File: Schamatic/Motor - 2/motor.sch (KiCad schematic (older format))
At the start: 60 parts, among them J1 CONN_02X05, J11 V, J12 U, J13 W, J3 RS485, J6 +BAT, J9 GND, Q1 PSMN3R3-40YS, Q2 PSMN3R3-40YS, Q3 PSMN3R3-40YS, Q4 PSMN3R3-40YS, Q5 PSMN3R3-40YS, Q6 PSMN3R3-40YS, Q7 NTR5103N, SW1 B3U-1000P, SW2 B3U-1000P, U1 MAX17502, U2 LTC2876, U3 MA700, U4 LM5019, U5 STM32F031K6U6, U6 AUIRS20302, Y1 8MhZ

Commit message: progress
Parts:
- removed C12: 3300pF, Capacitors_SMD:C_0603, symbol C_Small
- removed C13: 22uF, Capacitors_SMD:C_0805, symbol C_Small
- removed C8: 0.1uF, Capacitors_SMD:C_0603, symbol C_Small
- removed L1: 15uH, Inductors_SMD:L_1210, symbol L_Small
- removed U1: MAX17502, Housings_DFN_QFN:DFN-10-1EP_2x3mm_Pitch0.5mm, symbol MAX17502
- removed U3: MA700, Housings_DFN_QFN:QFN-16-1EP_3x3mm_Pitch0.5mm, symbol MA700
- added C2: 0.1uF, Capacitors_SMD:C_0603, symbol C_Small
- added U1: TPS73433DRV, Housings_DFN_QFN:DFN-6-1EP_2x2mm_Pitch0.65mm, symbol TPS73433DRV
- added U3: A1335, Housings_SSOP:TSSOP-14_4.4x5mm_Pitch0.65mm, symbol A1335
- C1: value 1uF -> 0.1uF
- Q7: footprint (none) -> TO_SOT_Packages_SMD:SOT-323_SC-70
- R12: value 230K -> 30k 1%
- R13: value 10K -> 10K 1%
- R15: value 390 -> 600
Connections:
- net labels added: +5V, DRV
- net labels removed: +24V
- wire segments 119 -> 114
- no-connect marks 13 -> 1
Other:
- moved on the sheet: C10, C11, C3, C9, D4, D7, L2, R10, R12, R13, R14, R15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

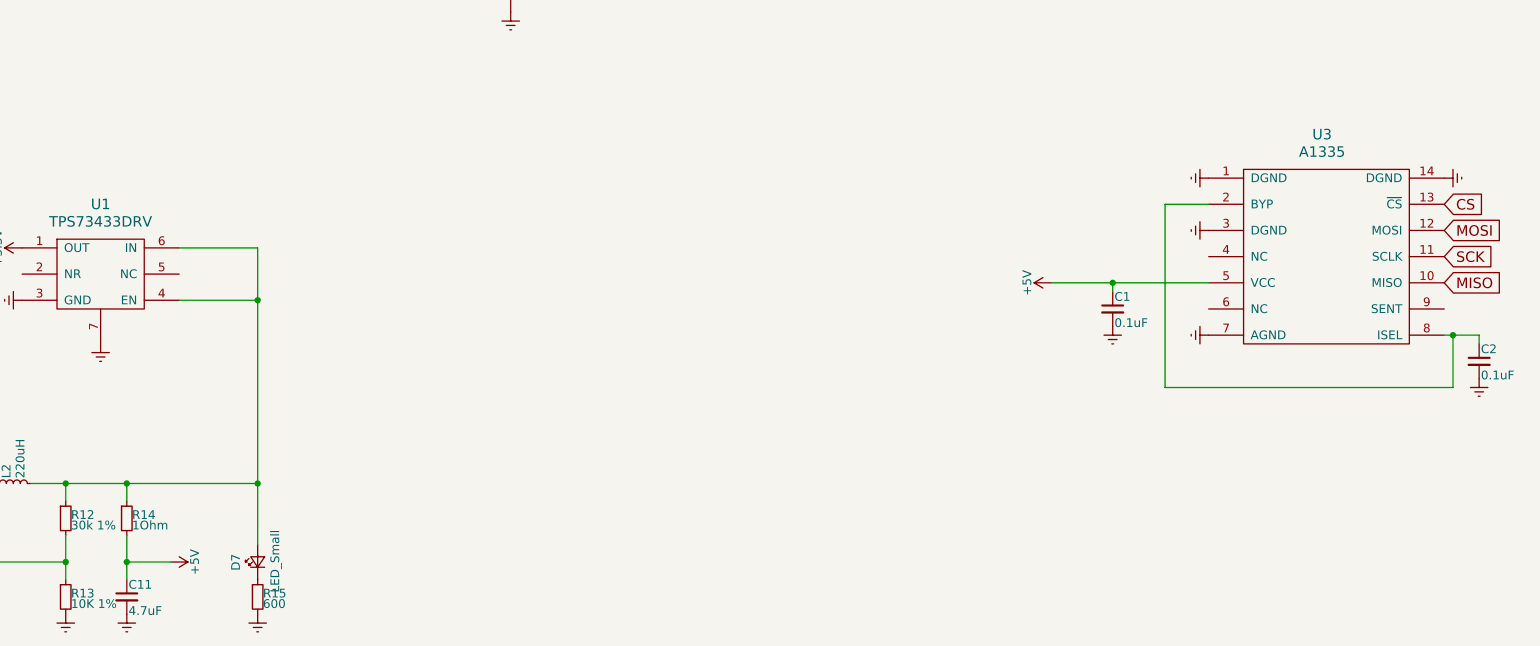
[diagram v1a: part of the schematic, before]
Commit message: 3.3V MA700
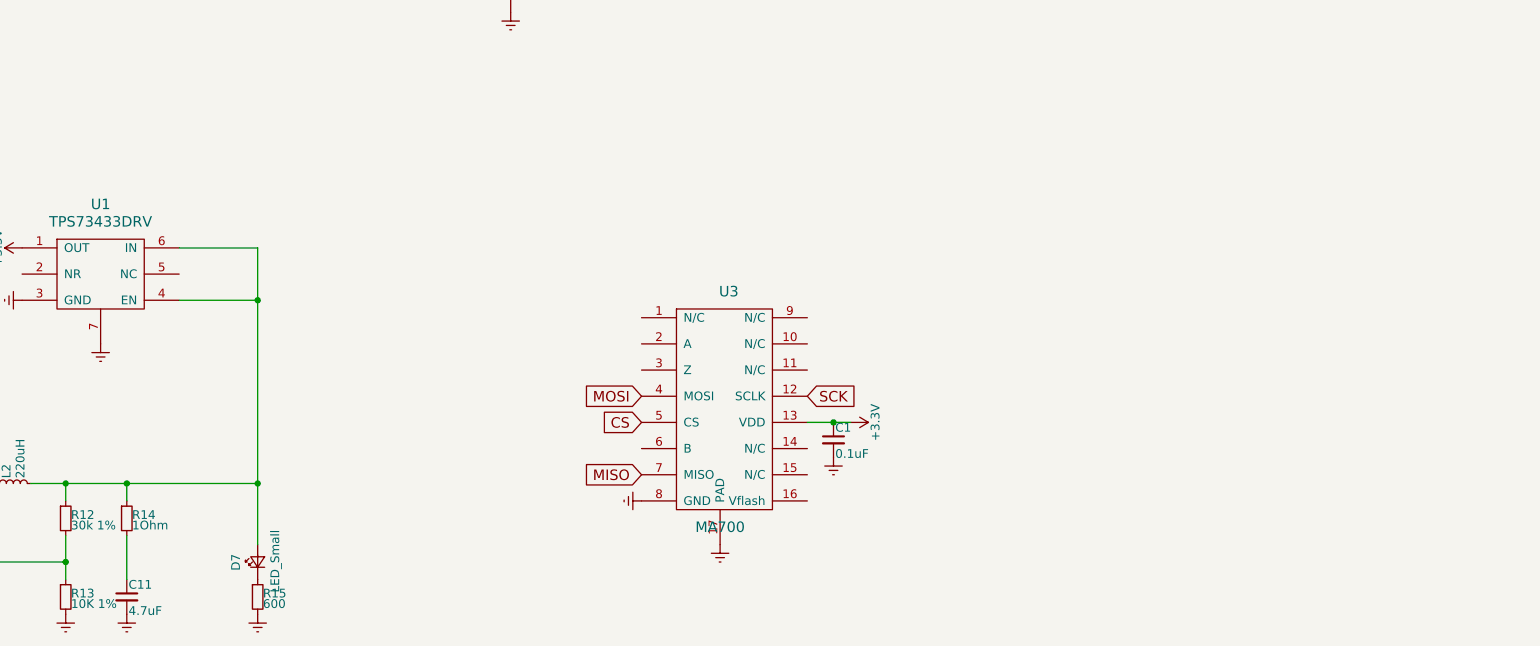
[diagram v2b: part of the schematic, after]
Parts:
- removed C2: 0.1uF, Capacitors_SMD:C_0603, symbol C_Small
- removed U3: A1335, Housings_SSOP:TSSOP-14_4.4x5mm_Pitch0.65mm, symbol A1335
- added U3: MA700, Housings_DFN_QFN:UQFN-16-1EP_3x3mm_Pitch0.5mm, symbol MA700
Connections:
- net +3V3: now also C1.1, U3.13 (VDD)
- net CS: now also U3.5 (CS)
- net Earth: now also U3.17 (PAD), U3.8 (GND)
- net MISO: now also U3.7 (MISO)
- net MOSI: now also U3.4 (MOSI)
- net SCK: now also U3.12 (SCLK)
- net +5V: no longer names the net of C11.1, R14.2
- net +5V: no longer C1.1
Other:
- moved on the sheet: C1
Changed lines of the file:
@@
 L1
 $Comp
-L +3.3V #PWR40
+L +3.3V #PWR39
 U 1 1 5977764D
 P 7050 5000
-F 0 "#PWR40" H 7050 4850 50  0001 C CNN
+F 0 "#PWR39" H 7050 4850 50  0001 C CNN
 F 1 "+3.3V" H 7050 5140 50  0000 C CNN
 F 2 "" H 7050 5000 50  0001 C CNN
@@
 $EndComp
 $Comp
-L Earth #PWR36
+L Earth #PWR34
 U 1 1 5977767B
 P 6650 5450
-F 0 "#PWR36" H 6650 5200 50  0001 C CNN
+F 0 "#PWR34" H 6650 5200 50  0001 C CNN
 F 1 "Earth" H 6650 5300 50  0001 C CNN
 F 2 "" H 6650 5450 50  0001 C CNN
@@
 $EndComp
 $Comp
-L Earth #PWR37
+L Earth #PWR35
 U 1 1 59CA6988
 P 6850 4800
-F 0 "#PWR37" H 6850 4550 50  0001 C CNN
+F 0 "#PWR35" H 6850 4550 50  0001 C CNN
 F 1 "Earth" H 6850 4650 50  0001 C CNN
 F 2 "" H 6850 4800 50  0001 C CNN
@@
 $EndComp
 $Comp
-L Earth #PWR35
+L Earth #PWR33
 U 1 1 5A06E0D7
 P 6200 5700
-F 0 "#PWR35" H 6200 5450 50  0001 C CNN
+F 0 "#PWR33" H 6200 5450 50  0001 C CNN
 F 1 "Earth" H 6200 5550 50  0001 C CNN
 F 2 "" H 6200 5700 50  0001 C CNN
@@
 LIN3
 $Comp
-L Earth #PWR33
+L Earth #PWR31
 U 1 1 5B1C6C81
 P 5900 3300
-F 0 "#PWR33" H 5900 3050 50  0001 C CNN
+F 0 "#PWR31" H 5900 3050 50  0001 C CNN
 F 1 "Earth" H 5900 3150 50  0001 C CNN
 F 2 "" H 5900 3300 50  0001 C CNN
@@
 $EndComp
 $Comp
-L Earth #PWR34
+L Earth #PWR32
 U 1 1 5B1C6D16
 P 5900 4200
-F 0 "#PWR34" H 5900 3950 50  0001 C CNN
+F 0 "#PWR32" H 5900 3950 50  0001 C CNN
 F 1 "Earth" H 5900 4050 50  0001 C CNN
 F 2 "" H 5900 4200 50  0001 C CNN
@@
 $EndComp
 $Comp
-L +3.3V #PWR30
+L +3.3V #PWR29
 U 1 1 5B1D570A
 P 4850 3400
-F 0 "#PWR30" H 4850 3250 50  0001 C CNN
+F 0 "#PWR29" H 4850 3250 50  0001 C CNN
 F 1 "+3.3V" V 4750 3450 50  0000 C CNN
 F 2 "" H 4850 3400 50  0001 C CNN
@@
 $EndComp
 $Comp
-L Earth #PWR31
+L Earth #PWR30
 U 1 1 5B1D594A
 P 4900 3550
-F 0 "#PWR31" H 4900 3300 50  0001 C CNN
+F 0 "#PWR30" H 4900 3300 50  0001 C CNN
 F 1 "Earth" H 4900 3400 50  0001 C CNN
 F 2 "" H 4900 3550 50  0001 C CNN
@@
 $EndComp
 $Comp
-L Earth #PWR29
+L Earth #PWR28
 U 1 1 5B1E4188
 P 4750 9150
-F 0 "#PWR29" H 4750 8900 50  0001 C CNN
+F 0 "#PWR28" H 4750 8900 50  0001 C CNN
 F 1 "Earth" H 4750 9000 50  0001 C CNN
 F 2 "" H 4750 9150 50  0001 C CNN
@@
 	4750 7050 4750 8750
 $Comp
-L +3.3V #PWR38
+L +3.3V #PWR37
 U 1 1 5B1EA425
 P 7050 3900
-F 0 "#PWR38" H 7050 3750 50  0001 C CNN
+F 0 "#PWR37" H 7050 3750 50  0001 C CNN
 F 1 "+3.3V" H 7050 4040 50  0000 C CNN
 F 2 "" H 7050 3900 50  0001 C CNN
@@
 $EndComp
 $Comp
-L Earth #PWR39
+L Earth #PWR38
 U 1 1 5B1EA5C0
 P 7050 4050
-F 0 "#PWR39" H 7050 3800 50  0001 C CNN
+F 0 "#PWR38" H 7050 3800 50  0001 C CNN
 F 1 "Earth" H 7050 3900 50  0001 C CNN
 F 2 "" H 7050 4050 50  0001 C CNN
@@
 $EndComp
 $Comp
-L +5V #PWR28
-U 1 1 5B34DD41
-P 4250 8850
-F 0 "#PWR28" H 4250 8700 50  0001 C CNN
-F 1 "+5V" H 4250 8990 50  0000 C CNN
-F 2 "" H 4250 8850 50  0001 C CNN
-F 3 "" H 4250 8850 50  0001 C CNN
-	1    4250 8850
-	0    1    1    0
-$EndComp
-Wire Wire Line
-	4250 8850 4000 8850
-Connection ~ 4000 8850
-$Comp
 L TPS73433DRV U1
 U 1 1 5B34E3F5
@@
 $EndComp
 $Comp
-L A1335 U3
-U 1 1 5B358114
-P 10850 6500
-F 0 "U3" H 10850 6600 60  0000 C CNN
-F 1 "A1335" H 10850 6500 60  0000 C CNN
-F 2 "Housings_SSOP:TSSOP-14_4.4x5mm_Pitch0.65mm" H 10850 6500 60  0001 C CNN
-F 3 "" H 10850 6500 60  0001 C CNN
-	1    10850 6500
-	1    0    0    -1
-$EndComp
-Wire Wire Line
-	9950 7850 11600 7850
-Wire Wire Line
-	9950 7850 9950 6800
-Wire Wire Line
-	9950 6800 10200 6800
-$Comp
-L C_Small C2
-U 1 1 5B358900
-P 11750 7700
-F 0 "C2" H 11760 7770 50  0000 L CNN
-F 1 "0.1uF" H 11760 7620 50  0000 L CNN
-F 2 "Capacitors_SMD:C_0603" H 11750 7700 50  0001 C CNN
-F 3 "" H 11750 7700 50  0001 C CNN
-	1    11750 7700
-	1    0    0    -1
-$EndComp
-Wire Wire Line
-	11750 7600 11750 7550
-Wire Wire Line
-	11750 7550 11550 7550
-$Comp
-L Earth #PWR53
+L Earth #PWR40
 U 1 1 5B358B72
-P 11750 7800
-F 0 "#PWR53" H 11750 7550 50  0001 C CNN
-F 1 "Earth" H 11750 7650 50  0001 C CNN
-F 2 "" H 11750 7800 50  0001 C CNN
-F 3 "" H 11750 7800 50  0001 C CNN
-	1    11750 7800
-	1    0    0    -1
-$EndComp
-Wire Wire Line
-	11600 7850 11600 7550
-Connection ~ 11600 7550
+P 7400 8750
+F 0 "#PWR40" H 7400 8500 50  0001 C CNN
+F 1 "Earth" H 7400 8600 50  0001 C CNN
+F 2 "" H 7400 8750 50  0001 C CNN
+F 3 "" H 7400 8750 50  0001 C CNN
+	1    7400 8750
+	1    0    0    -1
+$EndComp
 $Comp
 L C_Small C1
 U 1 1 5B35926B
-P 9650 7400
-F 0 "C1" H 9660 7470 50  0000 L CNN
-F 1 "0.1uF" H 9660 7320 50  0000 L CNN
-F 2 "Capacitors_SMD:C_0603" H 9650 7400 50  0001 C CNN
-F 3 "" H 9650 7400 50  0001 C CNN
-	1    9650 7400
-	1    0    0    -1
-$EndComp
-$Comp
-L +5V #PWR41
-U 1 1 5B35A1CF
-P 9300 7250
-F 0 "#PWR41" H 9300 7100 50  0001 C CNN
-F 1 "+5V" H 9300 7390 50  0000 C CNN
-F 2 "" H 9300 7250 50  0001 C CNN
-F 3 "" H 9300 7250 50  0001 C CNN
-	1    9300 7250
-	0    -1   -1   0
-$EndComp
-Wire Wire Line
-	9300 7250 10200 7250
-Wire Wire Line
-	9650 7300 9650 7250
-Connection ~ 9650 7250
-$Comp
-L Earth #PWR42
+P 8050 8150
+F 0 "C1" H 8060 8220 50  0000 L CNN
+F 1 "0.1uF" H 8060 8070 50  0000 L CNN
+F 2 "Capacitors_SMD:C_0603" H 8050 8150 50  0001 C CNN
+F 3 "" H 8050 8150 50  0001 C CNN
+	1    8050 8150
+	1    0    0    -1
+$EndComp
+$Comp
+L Earth #PWR41
 U 1 1 5B35AFE4
-P 9650 7500
-F 0 "#PWR42" H 9650 7250 50  0001 C CNN
-F 1 "Earth" H 9650 7350 50  0001 C CNN
-F 2 "" H 9650 7500 50  0001 C CNN
-F 3 "" H 9650 7500 50  0001 C CNN
-	1    9650 7500
-	1    0    0    -1
-$EndComp
-Text GLabel 11550 6800 2    60   Input ~ 0
+P 8050 8250
+F 0 "#PWR41" H 8050 8000 50  0001 C CNN
+F 1 "Earth" H 8050 8100 50  0001 C CNN
+F 2 "" H 8050 8250 50  0001 C CNN
+F 3 "" H 8050 8250 50  0001 C CNN
+	1    8050 8250
+	1    0    0    -1
+$EndComp
+Text GLabel 6950 8050 0    60   Input ~ 0
 CS
-Text GLabel 11550 7100 2    60   Input ~ 0
+Text GLabel 7900 7900 2    60   Input ~ 0
 SCK
-Text GLabel 11550 7250 2    60   Input ~ 0
-MISO
-Text GLabel 11550 6950 2    60   Input ~ 0
+Text GLabel 6950 7900 0    60   Input ~ 0
 MOSI
 $Comp
-L Earth #PWR51
-U 1 1 5B36130C
-P 10200 7550
-F 0 "#PWR51" H 10200 7300 50  0001 C CNN
-F 1 "Earth" H 10200 7400 50  0001 C CNN
-F 2 "" H 10200 7550 50  0001 C CNN
-F 3 "" H 10200 7550 50  0001 C CNN
-	1    10200 7550
-	0    1    1    0
-$EndComp
-$Comp
-L Earth #PWR50
-U 1 1 5B3613C2
-P 10200 6950
-F 0 "#PWR50" H 10200 6700 50  0001 C CNN
-F 1 "Earth" H 10200 6800 50  0001 C CNN
-F 2 "" H 10200 6950 50  0001 C CNN
-F 3 "" H 10200 6950 50  0001 C CNN
-	1    10200 6950
-	0    1    1    0
-$EndComp
-$Comp
-L Earth #PWR49
-U 1 1 5B36155C
-P 10200 6650
-F 0 "#PWR49" H 10200 6400 50  0001 C CNN
-F 1 "Earth" H 10200 6500 50  0001 C CNN
-F 2 "" H 10200 6650 50  0001 C CNN
-F 3 "" H 10200 6650 50  0001 C CNN
-	1    10200 6650
-	0    1    1    0
-$EndComp
-$Comp
-L Earth #PWR52
+L Earth #PWR36
 U 1 1 5B361612
-P 11550 6650
-F 0 "#PWR52" H 11550 6400 50  0001 C CNN
-F 1 "Earth" H 11550 6500 50  0001 C CNN
-F 2 "" H 11550 6650 50  0001 C CNN
-F 3 "" H 11550 6650 50  0001 C CNN
-	1    11550 6650
-	0    -1   -1   0
+P 6950 8500
+F 0 "#PWR36" H 6950 8250 50  0001 C CNN
+F 1 "Earth" H 6950 8350 50  0001 C CNN
+F 2 "" H 6950 8500 50  0001 C CNN
+F 3 "" H 6950 8500 50  0001 C CNN
+	1    6950 8500
+	0    1    1    0
 $EndComp
 $Comp
@@
 Text GLabel 1300 8300 1    60   Input ~ 0
 DRV
+$Comp
+L MA700 U3
+U 1 1 5B36E594
+P 7450 8250
+F 0 "U3" H 7450 9200 60  0000 C CNN
+F 1 "MA700" H 7400 7850 60  0000 C CNN
+F 2 "Housings_DFN_QFN:UQFN-16-1EP_3x3mm_Pitch0.5mm" H 7450 8250 60  0001 C CNN
+F 3 "" H 7450 8250 60  0001 C CNN
+	1    7450 8250
+	1    0    0    -1
+$EndComp
+$Comp
+L +3.3V #PWR42
+U 1 1 5B36F7BF
+P 8150 8050
+F 0 "#PWR42" H 8150 7900 50  0001 C CNN
+F 1 "+3.3V" H 8150 8190 50  0000 C CNN
+F 2 "" H 8150 8050 50  0001 C CNN
+F 3 "" H 8150 8050 50  0001 C CNN
+	1    8150 8050
+	0    1    1    0
+$EndComp
+Wire Wire Line
+	7900 8050 8150 8050
+Connection ~ 8050 8050
+Text GLabel 6950 8350 0    60   Input ~ 0
+MISO
 $EndSCHEMATC

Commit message: changes
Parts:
- added C?: 2.2uF 25V, symbol C_Small
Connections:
- net Earth: now also C?.2
- net at D3.2 (A), D5.2 (A), D6.2 (A)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: now also C?.1
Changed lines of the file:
@@
 Text GLabel 6950 8350 0    60   Input ~ 0
 MISO
+$Comp
+L C_Small C?
+U 1 1 5B4340EB
+P 5850 1850
+F 0 "C?" H 5860 1920 50  0000 L CNN
+F 1 "2.2uF 25V" H 5860 1770 50  0000 L CNN
+F 2 "" H 5850 1850 50  0001 C CNN
+F 3 "" H 5850 1850 50  0001 C CNN
+	1    5850 1850
+	1    0    0    -1
+$EndComp
+$Comp
+L Earth #PWR?
+U 1 1 5B434912
+P 5850 1950
+F 0 "#PWR?" H 5850 1700 50  0001 C CNN
+F 1 "Earth" H 5850 1800 50  0001 C CNN
+F 2 "" H 5850 1950 50  0001 C CNN
+F 3 "" H 5850 1950 50  0001 C CNN
+	1    5850 1950
+	1    0    0    -1
+$EndComp
+Wire Wire Line
+	5850 1750 5850 1650
+Connection ~ 5850 1650
 $EndSCHEMATC

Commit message: new drivers
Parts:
- removed C?: 2.2uF 25V, symbol C_Small
- removed Q1, Q3, Q5: PSMN3R3-40YS, Dizzy:PSMN3R3-40YS, symbol PSMN014-40YS
- removed Q2, Q4, Q6: PSMN3R3-40YS, Dizzy:PSMN3R3-40YS-vias, symbol PSMN014-40YS
- removed Q7: NTR5103N, TO_SOT_Packages_SMD:SOT-323_SC-70, symbol Q_NMOS_GSD
- removed R3, R4, R5, R6, R7, R8: 10, Resistors_SMD:R_0603, symbol R
- removed R9: 100K, Resistors_SMD:R_0603, symbol R_Small
- removed U3: MA700, Housings_DFN_QFN:UQFN-16-1EP_3x3mm_Pitch0.5mm, symbol MA700
- removed U6: AUIRS20302, Housings_SOIC:SOIC-28W_7.5x18.7mm_Pitch1.27mm, symbol AUIRS20302
- added C12: 0.1uF, Capacitors_SMD:C_0603, symbol C_Small
- added C2, C8: 1uF, Capacitors_SMD:C_0603, symbol C_Small
- added D8: D_Small, Diodes_SMD:D_SOD-323F, symbol D_Small
- added J2: RS485, Pin_Headers:Pin_Header_Straight_1x02_Pitch2.54mm, symbol CONN_01X02
- added U3: ZXTR2012Z, TO_SOT_Packages_SMD:SOT-89-3, symbol MCP1703A-1502/MB
- added U6: A1335, Housings_SSOP:TSSOP-14_4.4x5mm_Pitch0.65mm, symbol A1335
- added U7, U8, U9: IRSM005, Dizzy:IRSM005, symbol IRSM005
- C6: value 1uF -> 0.1uF
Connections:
- net +3V3: now also C12.1; no longer C1.1
- net +BATT: now also U7.13 (V+), U8.13 (V+), U9.13 (V+)
- net CS: now also U6.13 (~CS)
- net Earth: now also C6.2, C12.2, C2.2, U3.1 (GND), U6.1 (DGND), U6.14 (DGND), U6.3 (DGND), U6.7 (AGND), U7.11 (V-), U7.28, U7.3, U7.6 (COM), U7.8, U8.11 (V-), U8.28, U8.3, U8.6 (COM), U8.8, U9.11 (V-), U9.28, U9.3, U9.6 (COM), U9.8
- net HIN1: now also U7.4 (HIN)
- net HIN2: now also U8.4 (HIN)
- net HIN3: now also U9.4 (HIN)
- net LIN1: now also U7.5 (LIN)
- net LIN2: now also U8.5 (LIN)
- net LIN3: now also U9.5 (LIN)
- net MISO: now also U6.10 (MISO)
- net MOSI: now also U6.12 (MOSI)
- net RS-A: now also J2.2 (P2)
- net RS-B: now also J2.1 (P1)
- net SCK: now also U6.11 (SCLK)
- net at D7.2 (A), L2.2, R12.1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: now also D8.2 (A)
- net 12V: now reaches D3.2 (A), D5.2 (A), D6.2 (A)
- net 12V: now also C2.1, U3.3 (VO), U7.2 (VCC), U8.2 (VCC), U9.2 (VCC)
- net BOOT1: no longer names the net of C4.1
- net BOOT1: now also U7.26 (VS), U7.27; no longer D3.1 (K)
- net BOOT2: no longer names the net of C5.1
- net BOOT2: now also U8.26 (VS), U8.27; no longer D5.1 (K)
- net BOOT3: no longer names the net of D6.1 (K)
- net BOOT3: now also C8.2, U9.1 (VB); no longer C6.1
- net DRV: no longer names the net of C3.1, D4.1 (K), R10.2, U4.2 (VIN), U4.3 (UVLO)
- net DRV: now also U3.2 (VI)
- net O1: no longer names the net of C4.2
- net O1: now also D3.1 (K), U7.1 (VB); no longer J11.1 (P1)
- net O2: no longer names the net of C5.2
- net O2: now also D5.1 (K), U8.1 (VB); no longer J12.1 (P1)
- net O3: no longer names the net of J13.1 (P1)
- net O3: now also U9.10 (VS), U9.12; no longer C6.2
- new net: J11.1 (P1), U7.10 (VS), U7.12
- new net: J12.1 (P1), U8.10 (VS), U8.12
- new net: U7.24 (G1), U7.25 (HO)
- new net: U7.7 (LO), U7.9 (G2)
- new net: U8.24 (G1), U8.25 (HO)
- new net: U8.7 (LO), U8.9 (G2)
- new net: U9.24 (G1), U9.25 (HO)
- new net: C8.1, U9.26 (VS), U9.27
- new net: U9.7 (LO), U9.9 (G2)
- new net: C6.1, U6.2 (BYP), U6.8 (ISEL)
- new net 5V: C1.1, D8.1 (K), U6.5 (VCC)
- no-connect marks 1 -> 0
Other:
- moved on the sheet: C1, C4, C5, D3, D5, D6, J11, J12, J13
